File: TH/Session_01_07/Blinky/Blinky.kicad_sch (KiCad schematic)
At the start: 12 parts

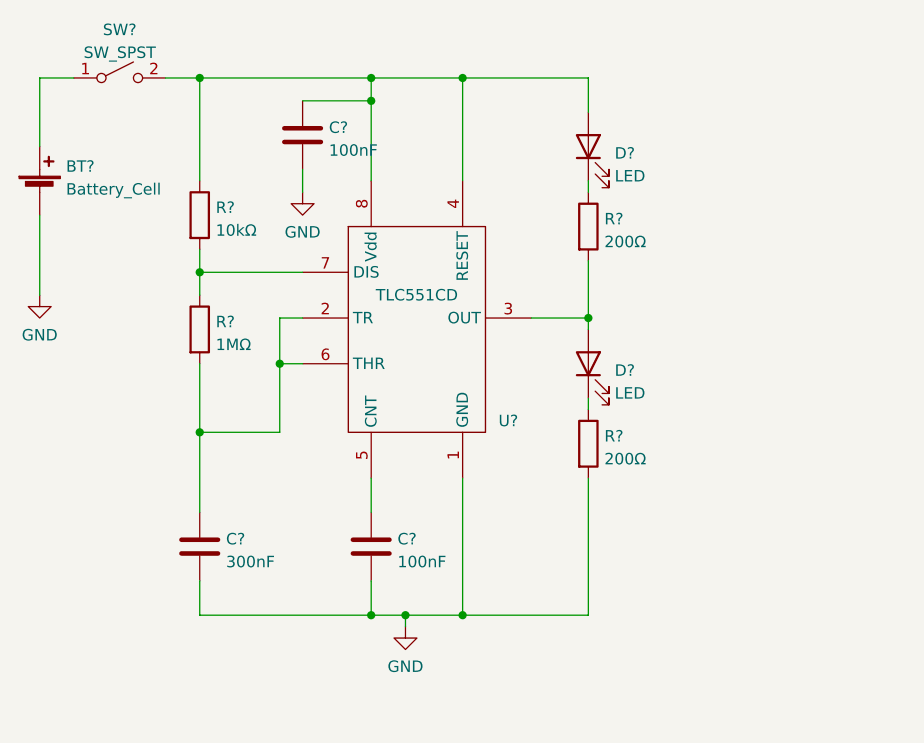
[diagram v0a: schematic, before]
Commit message: Revamps the through-hole project as transistor based
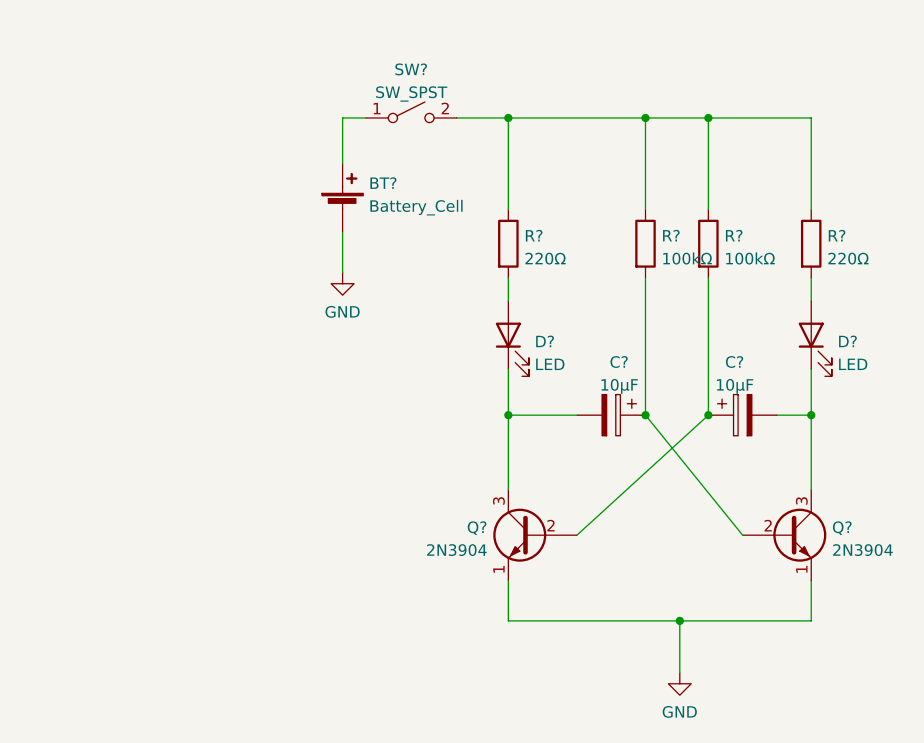
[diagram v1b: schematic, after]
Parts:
- removed BT?: Battery_Cell, symbol Device:Battery_Cell
- removed C? (x2): 100nF, Capacitor_THT:C_Disc_D5.0mm_W2.5mm_P5.00mm, symbol Device:C
- removed C?: 300nF, Capacitor_THT:C_Disc_D5.0mm_W2.5mm_P5.00mm, symbol Device:C
- removed D? (x2): LED, LED_THT:LED_D5.0mm, symbol Device:LED
- removed R? (x2): 200Ω, Resistor_THT:R_Axial_DIN0207_L6.3mm_D2.5mm_P10.16mm_Horizontal, symbol Device:R
- removed R?: 10kΩ, Resistor_THT:R_Axial_DIN0207_L6.3mm_D2.5mm_P10.16mm_Horizontal, symbol Device:R
- removed R?: 1MΩ, Resistor_THT:R_Axial_DIN0207_L6.3mm_D2.5mm_P10.16mm_Horizontal, symbol Device:R
- removed SW?: SW_SPST, symbol Switch:SW_SPST
- removed U?: TLC551CD‎, Package_DIP:DIP-8_W7.62mm_Socket, symbol Blinky:TLC551CD‎
- added BT?: Battery_Cell, symbol Device:Battery_Cell
- added C? (x2): 10μF, Capacitor_THT:CP_Radial_D5.0mm_P2.50mm, symbol Device:C_Polarized
- added D? (x2): LED, LED_THT:LED_D5.0mm, symbol Device:LED
- added Q? (x2): 2N3904, Package_TO_SOT_THT:TO-92_Inline, symbol Transistor_BJT:2N3904
- added R? (x2): 220Ω, Resistor_THT:R_Axial_DIN0207_L6.3mm_D2.5mm_P2.54mm_Vertical, symbol Device:R
- added R? (x2): 100kΩ, Resistor_THT:R_Axial_DIN0207_L6.3mm_D2.5mm_P2.54mm_Vertical, symbol Device:R
- added SW?: SW_SPST, symbol Switch:SW_SPST
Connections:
- net GND: now also BT?.2 (-), Q?.1 (E), Q?.1 (E)
- new net: R?.1, R?.1, R?.1, R?.1, SW?.2 (B)
- new net: D?.2 (A), R?.2 (x2)
- new net: C?.2, D?.1 (K), Q?.3 (C) (x2)
- new net: C?.1, Q?.2 (B), R?.2 (x2)
- new net: BT?.1 (+), SW?.1 (A)
